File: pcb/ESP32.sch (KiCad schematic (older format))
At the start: 1 part, among them U1 ESP32-WROOM

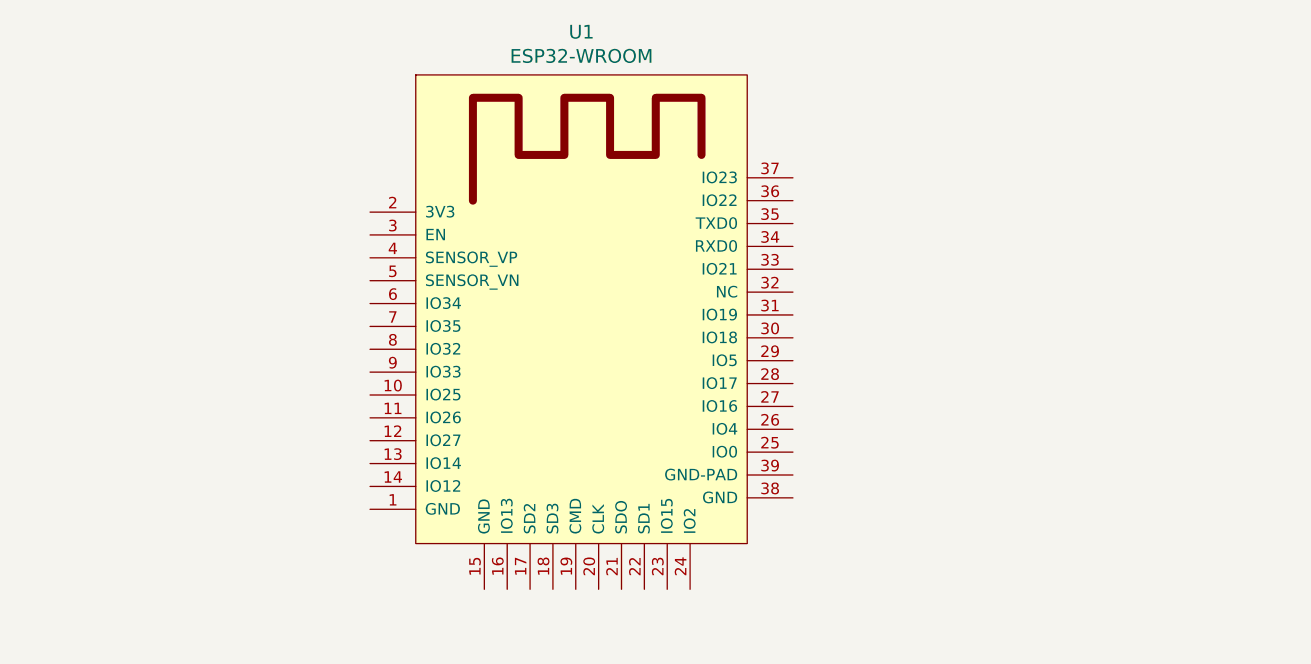
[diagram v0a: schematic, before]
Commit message: added barrel_connector and 3v3 reg libraries, added connections on supply sheet
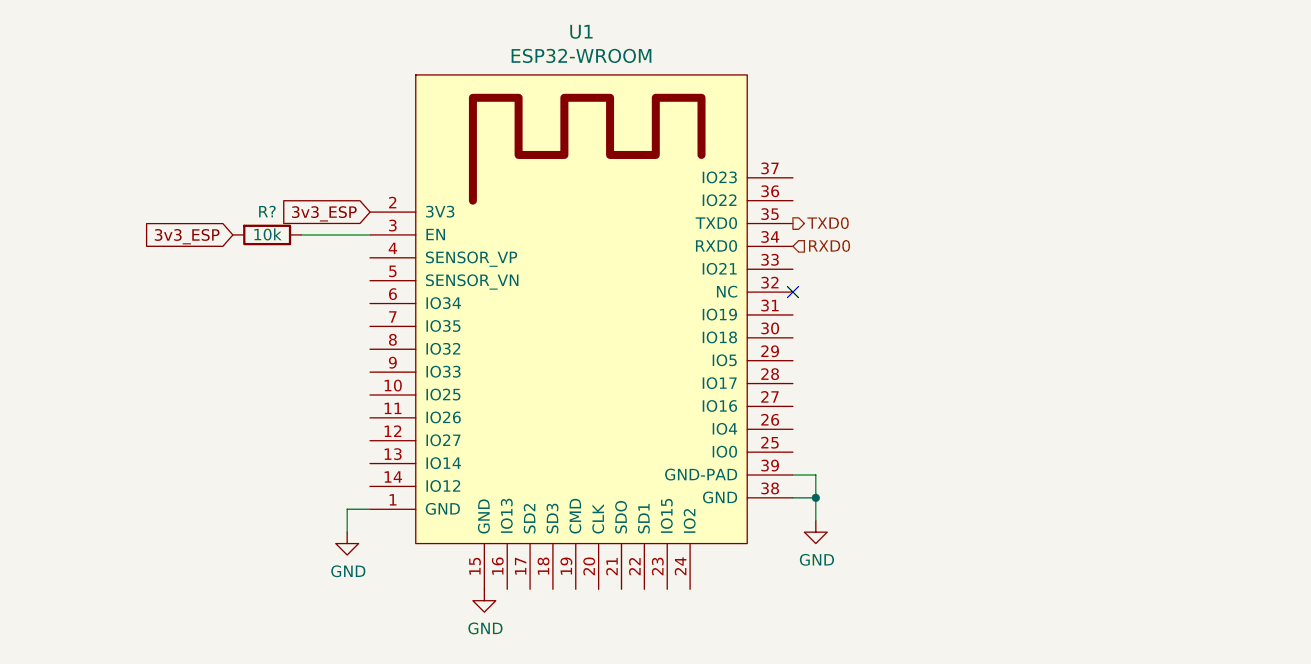
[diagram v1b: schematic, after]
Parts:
- added R?: 10k, symbol Device:R
- U1: Digikey (none) -> 1904-1010-1-ND
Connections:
- net GND: now reaches U1.1 (GND)
- net GND: now also U1.15 (GND), U1.38 (GND), U1.39 (GND-PAD)
- net 3v3_ESP: now reaches U1.2 (3V3)
- net 3v3_ESP: now also R?.2
- net at U1.3 (EN): now also R?.1
- net RXD0: now reaches U1.34 (RXD0)
- net TXD0: now reaches U1.35 (TXD0)
- no-connect marks 0 -> 1
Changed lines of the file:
@@
 F 1 "ESP32-WROOM" H 4225 4381 60  0000 C CNN
 F 2 "SMD:ESP32-WROOM" H 4600 4450 60  0001 C CNN
-F 3 "" H 3800 3550 60  0001 C CNN
+F 3 "https://www.espressif.com/sites/default/files/documentation/esp32-wroom-32_datasheet_en.pdf" H 3800 3550 60  0001 C CNN
+F 4 "1904-1010-1-ND" H 4250 3100 50  0001 C CNN "Digikey"
 	1    4250 3100
 	1    0    0    -1
 $EndComp
+NoConn ~ 5150 2850
+$Comp
+L power:GND #PWR?
+U 1 1 5E8F2039
+P 3800 4150
+F 0 "#PWR?" H 3800 3900 50  0001 C CNN
+F 1 "GND" H 3805 3977 50  0000 C CNN
+F 2 "" H 3800 4150 50  0001 C CNN
+F 3 "" H 3800 4150 50  0001 C CNN
+	1    3800 4150
+	1    0    0    -1
+$EndComp
+$Comp
+L power:GND #PWR?
+U 1 1 5E8F205E
+P 3200 3900
+F 0 "#PWR?" H 3200 3650 50  0001 C CNN
+F 1 "GND" H 3205 3727 50  0000 C CNN
+F 2 "" H 3200 3900 50  0001 C CNN
+F 3 "" H 3200 3900 50  0001 C CNN
+	1    3200 3900
+	1    0    0    -1
+$EndComp
+$Comp
+L power:GND #PWR?
+U 1 1 5E8F2083
+P 5250 3850
+F 0 "#PWR?" H 5250 3600 50  0001 C CNN
+F 1 "GND" H 5255 3677 50  0000 C CNN
+F 2 "" H 5250 3850 50  0001 C CNN
+F 3 "" H 5250 3850 50  0001 C CNN
+	1    5250 3850
+	1    0    0    -1
+$EndComp
+Wire Wire Line
+	5250 3850 5250 3750
+Wire Wire Line
+	5250 3750 5150 3750
+Wire Wire Line
+	3200 3900 3200 3800
+Wire Wire Line
+	3200 3800 3300 3800
+Wire Wire Line
+	5150 3650 5250 3650
+Wire Wire Line
+	5250 3650 5250 3750
+Connection ~ 5250 3750
+Text GLabel 3300 2500 0    50   Input ~ 0
+3v3_ESP
+$Comp
+L Device:R R?
+U 1 1 5E8F5CB8
+P 2850 2600
+F 0 "R?" V 2750 2600 50  0000 C CNN
+F 1 "10k" V 2850 2600 50  0000 C CNN
+F 2 "" V 2780 2600 50  0001 C CNN
+F 3 "~" H 2850 2600 50  0001 C CNN
+	1    2850 2600
+	0    1    1    0
+$EndComp
+Wire Wire Line
+	3000 2600 3300 2600
+Text GLabel 2700 2600 0    50   Input ~ 0
+3v3_ESP
+Text HLabel 5150 2550 2    50   Output ~ 0
+TXD0
+Text HLabel 5150 2650 2    50   Input ~ 0
+RXD0
 $EndSCHEMATC

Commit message: added power connections and a led
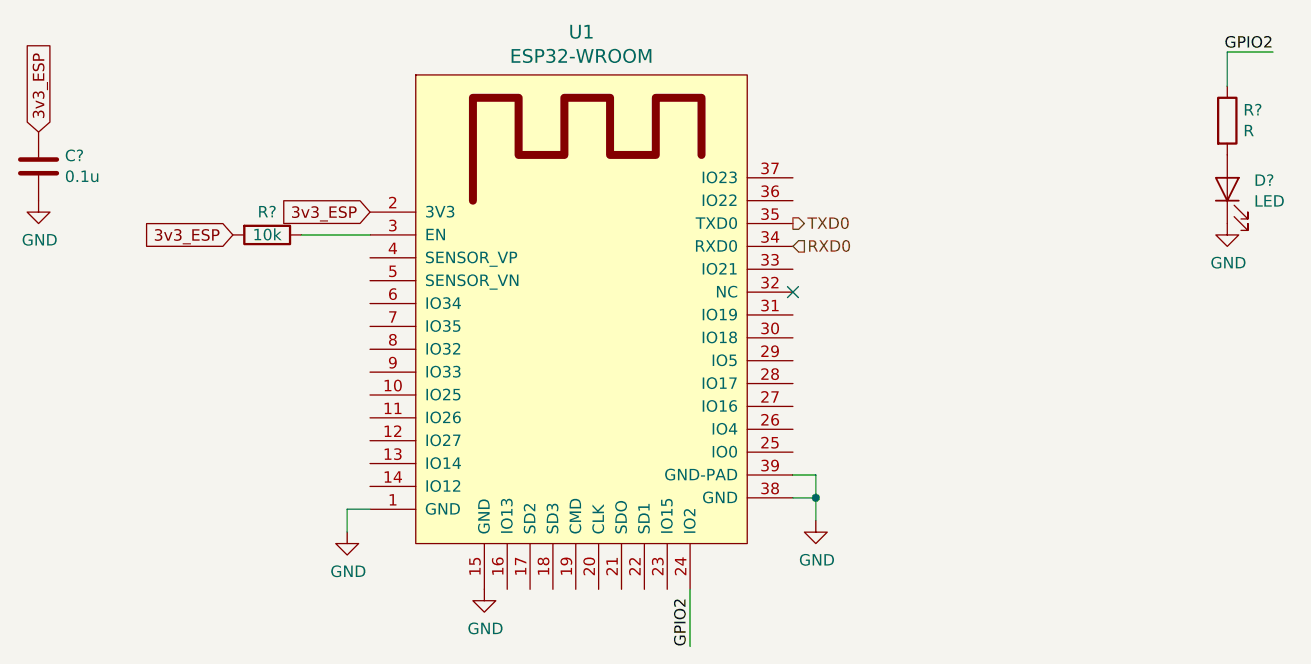
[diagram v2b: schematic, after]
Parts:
- added C?: 0.1u, symbol Device:C
- added D?: LED, symbol Device:LED
- added R?: R, symbol Device:R
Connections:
- net 3v3_ESP: now also C?.1
- net GND: now also C?.2, D?.1 (K)
- net GPIO2: now reaches U1.24 (IO2)
- net GPIO2: now also R?.1
- new net: D?.2 (A), R?.2
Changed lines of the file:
@@
 Text HLabel 5150 2650 2    50   Input ~ 0
 RXD0
+Text GLabel 1850 2150 1    50   Input ~ 0
+3v3_ESP
+$Comp
+L Device:C C?
+U 1 1 5E8E7E17
+P 1850 2300
+F 0 "C?" H 1965 2346 50  0000 L CNN
+F 1 "0.1u" H 1965 2255 50  0000 L CNN
+F 2 "" H 1888 2150 50  0001 C CNN
+F 3 "~" H 1850 2300 50  0001 C CNN
+	1    1850 2300
+	1    0    0    -1
+$EndComp
+$Comp
+L power:GND #PWR?
+U 1 1 5E8E7EAA
+P 1850 2450
+F 0 "#PWR?" H 1850 2200 50  0001 C CNN
+F 1 "GND" H 1855 2277 50  0000 C CNN
+F 2 "" H 1850 2450 50  0001 C CNN
+F 3 "" H 1850 2450 50  0001 C CNN
+	1    1850 2450
+	1    0    0    -1
+$EndComp
+$Comp
+L Device:R R?
+U 1 1 5E90464A
+P 7050 2100
+F 0 "R?" H 7120 2146 50  0000 L CNN
+F 1 "R" H 7120 2055 50  0000 L CNN
+F 2 "" V 6980 2100 50  0001 C CNN
+F 3 "~" H 7050 2100 50  0001 C CNN
+	1    7050 2100
+	1    0    0    -1
+$EndComp
+$Comp
+L Device:LED D?
+U 1 1 5E9046C5
+P 7050 2400
+F 0 "D?" V 7088 2283 50  0000 R CNN
+F 1 "LED" V 6997 2283 50  0000 R CNN
+F 2 "" H 7050 2400 50  0001 C CNN
+F 3 "~" H 7050 2400 50  0001 C CNN
+	1    7050 2400
+	0    -1   -1   0
+$EndComp
+$Comp
+L power:GND #PWR?
+U 1 1 5E904748
+P 7050 2550
+F 0 "#PWR?" H 7050 2300 50  0001 C CNN
+F 1 "GND" H 7055 2377 50  0000 C CNN
+F 2 "" H 7050 2550 50  0001 C CNN
+F 3 "" H 7050 2550 50  0001 C CNN
+	1    7050 2550
+	1    0    0    -1
+$EndComp
+Text Label 7250 1800 2    50   ~ 0
+GPIO2
+Wire Wire Line
+	7050 1800 7250 1800
+Wire Wire Line
+	7050 1800 7050 1950
+Text Label 4700 4400 1    50   ~ 0
+GPIO2
+Wire Wire Line
+	4700 4400 4700 4150
 $EndSCHEMATC
